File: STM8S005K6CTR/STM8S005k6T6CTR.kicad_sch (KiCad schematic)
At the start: 13 parts, among them IC1 STM8S005K6T6CTR, IC2 L6981C50DR, J1 282837-2

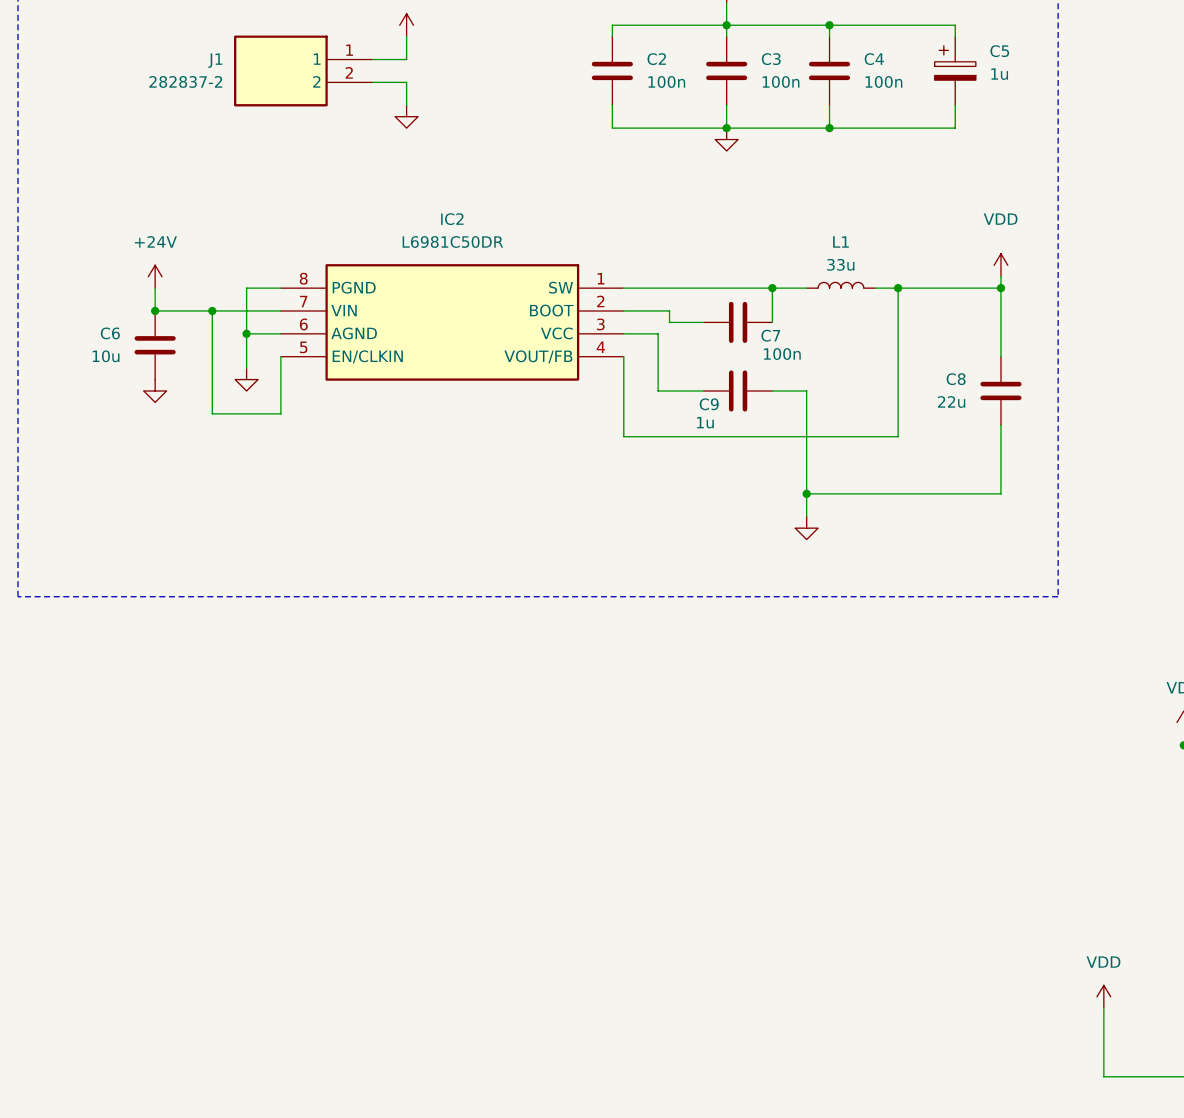
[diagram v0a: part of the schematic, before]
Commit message: [STM8S005K6T6CTR] Calculations: calculated values of components for switching voltage regulator - TI LM2671. Board scheme: Added switching voltage regulator with additional components. Assigned footprints to components.
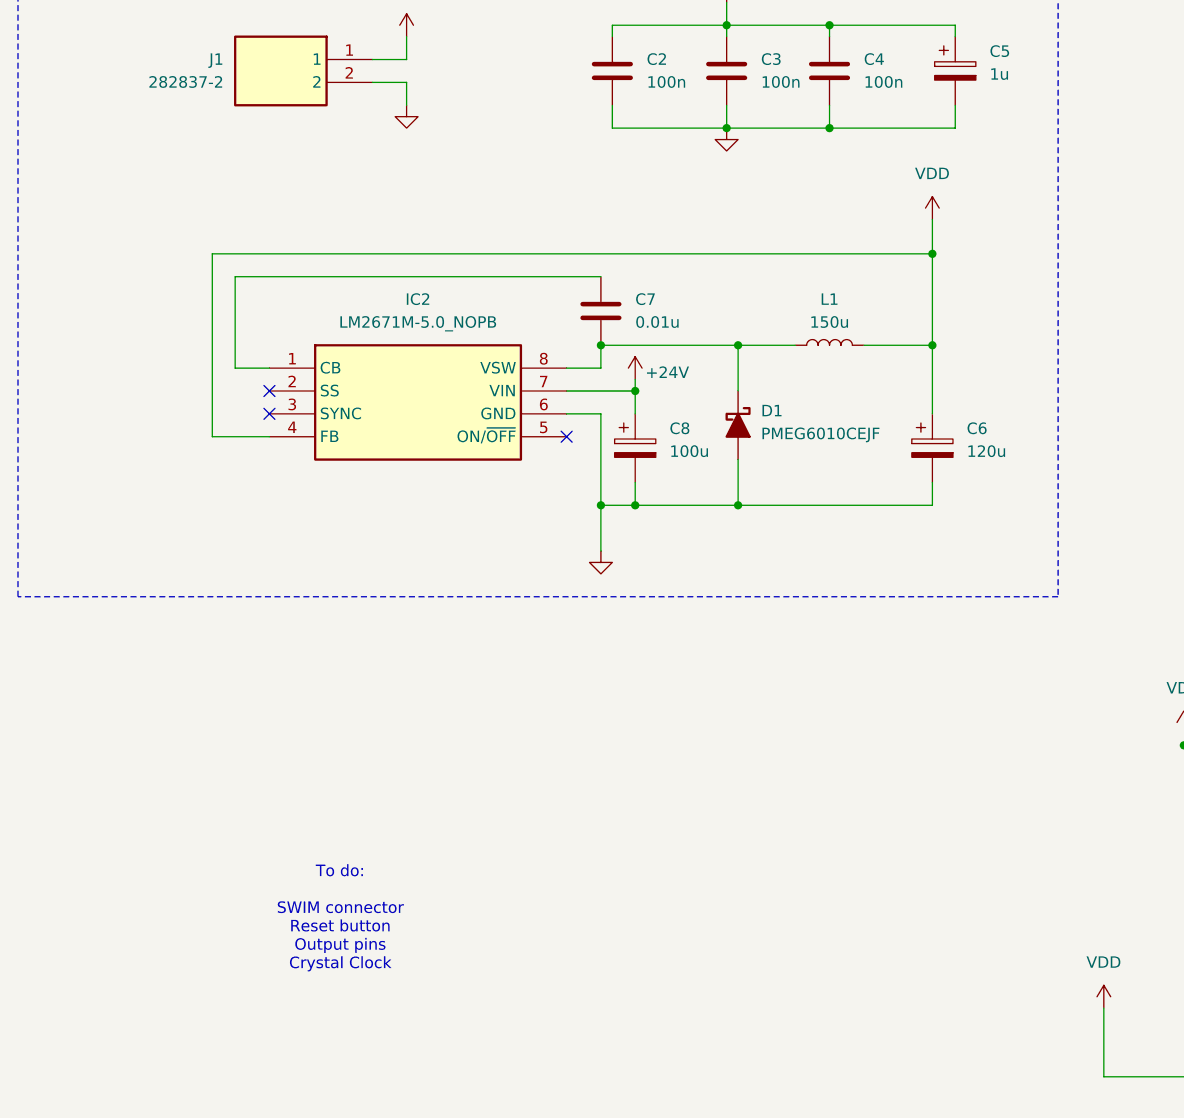
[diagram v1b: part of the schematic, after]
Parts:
- removed C6: 10u, symbol Device:C
- removed C8: 22u, symbol Device:C
- removed C9: 1u, symbol Device:C
- removed IC2: L6981C50DR, SOIC127P600X175-8N, symbol L6981C50DR:L6981C50DR
- added C6: 120u, Capacitor_THT:CP_Radial_D10.0mm_P5.00mm, symbol Device:C_Polarized
- added C8: 100u, Capacitor_THT:CP_Radial_D10.0mm_P5.00mm, symbol Device:C_Polarized
- added D1: PMEG6010CEJF, Diode_SMD:D_SOD-323F, symbol Device:D_Schottky_Filled
- added IC2: LM2671M-5.0_NOPB, SOIC127P600X175-8N, symbol LM2671M-5_0_NOPB:LM2671M-5.0_NOPB
- C7: value 100n -> 0.01u; footprint (none) -> Capacitor_SMD:C_0603_1608Metric
- L1: value 33u -> 150u; footprint (none) -> Wurth_744065151:WE-TPC_1028_103892
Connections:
- net +24V: now also C8.1, IC2.7 (VIN)
- net GND: now also C6.1, C6.2, C8.2, D1.2 (A), IC2.4 (FB), IC2.6 (GND)
- net at C7.2: now also IC2.1 (CB); no longer L1.1
- net at C7.1: now also L1.1, D1.1 (K), IC2.8 (VSW)
- no-connect marks 0 -> 3
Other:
- note added: "To do: SWIM connector Reset button Output pins Crystal Clock"

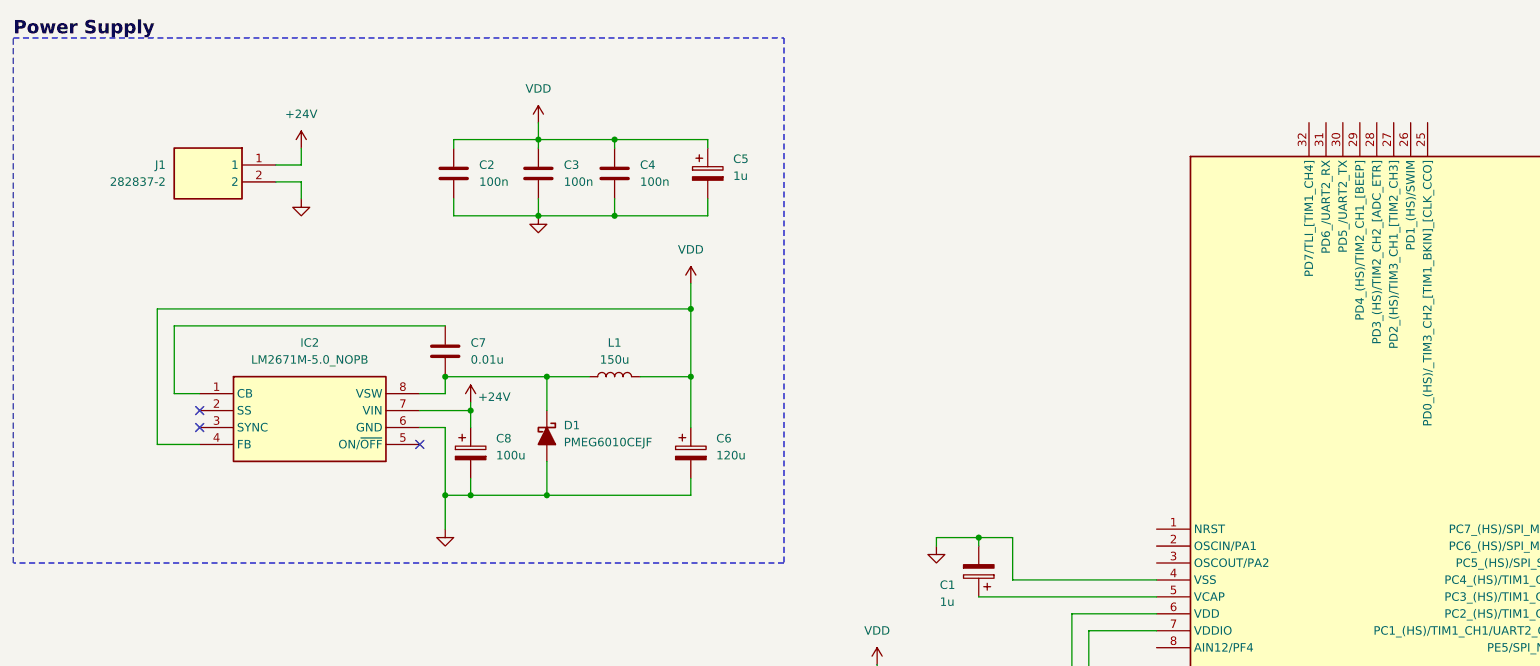
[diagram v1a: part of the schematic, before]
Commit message: [STM8S005K6T6CTR] Board scheme: Added Power Supply Selecection pins. Added SWIM connector.
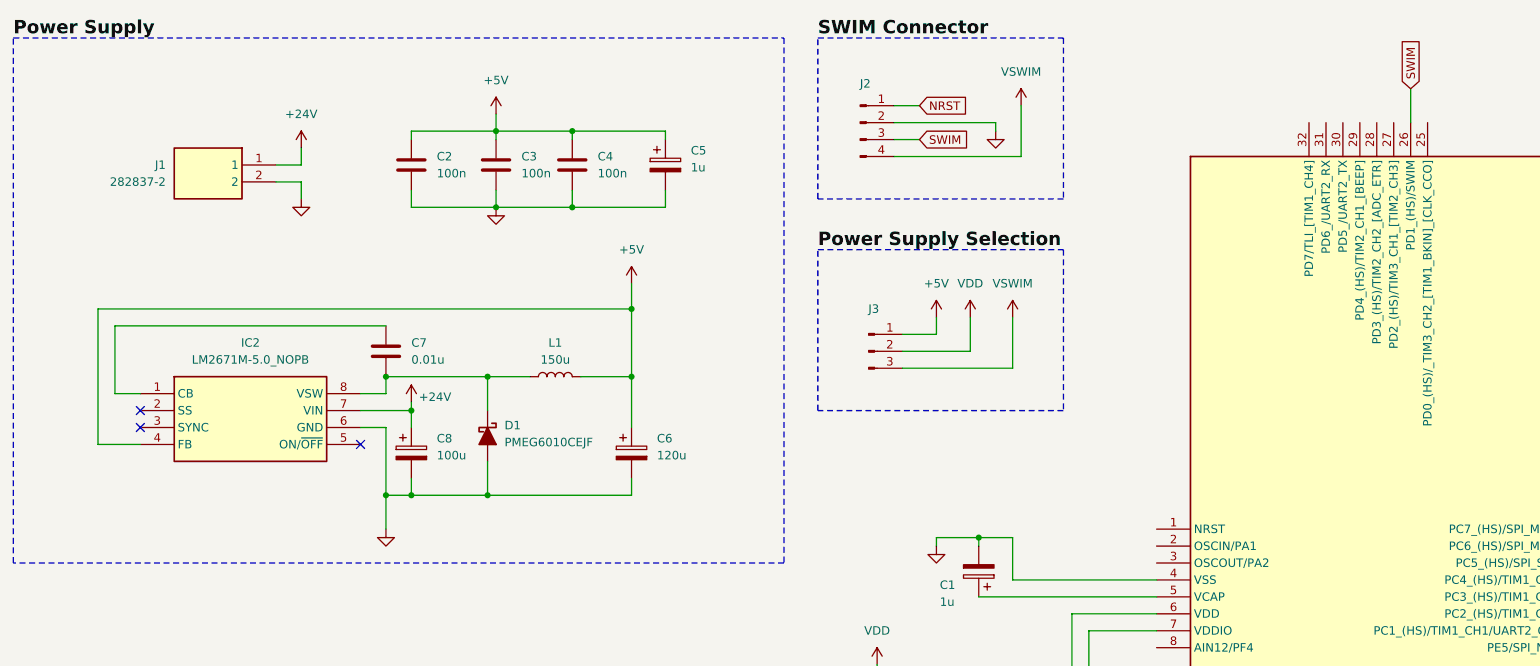
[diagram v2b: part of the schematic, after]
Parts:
- added J2: Conn_01x04_Pin, symbol Connector:Conn_01x04_Pin
- added J3: Conn_01x03_Pin, symbol Connector:Conn_01x03_Pin
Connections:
- net GND: now also J2.2 (Pin_2), J3.2 (Pin_2); no longer C2.1, C3.1, C4.1, C5.1, C6.1, IC2.4 (FB), L1.2
- net SWIM: now reaches IC1.26 (PD1_(HS)/SWIM)
- net SWIM: now also J2.3 (Pin_3)
- new net +5V: C2.1, C3.1, C4.1, C5.1, C6.1, IC2.4 (FB), J3.1 (Pin_1), L1.2
- new net NRST: J2.1 (Pin_1)
- new net VSWIM: J2.4 (Pin_4), J3.3 (Pin_3)
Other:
- moved on the sheet: C2, C3, C4, C5, C6, C7, C8, D1, IC2, L1

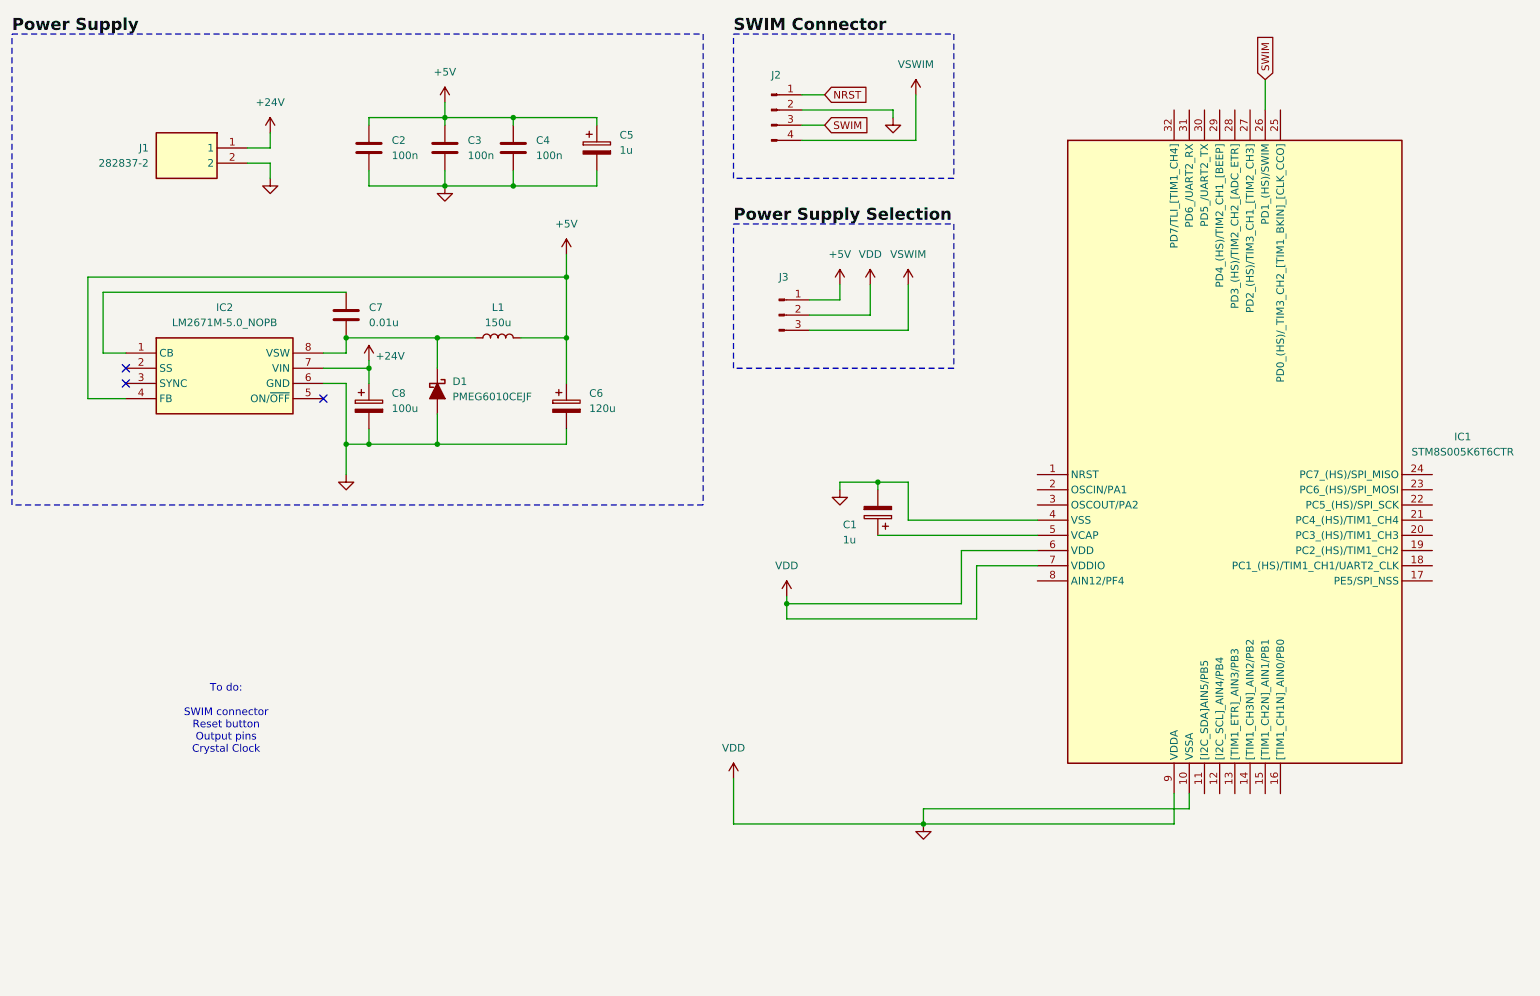
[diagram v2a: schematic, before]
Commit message: [STM8S005K6T6CTR] Calculations: calculated crystal components. Board scheme: Added crystal to scheme (with footprint). Added part of output pins.
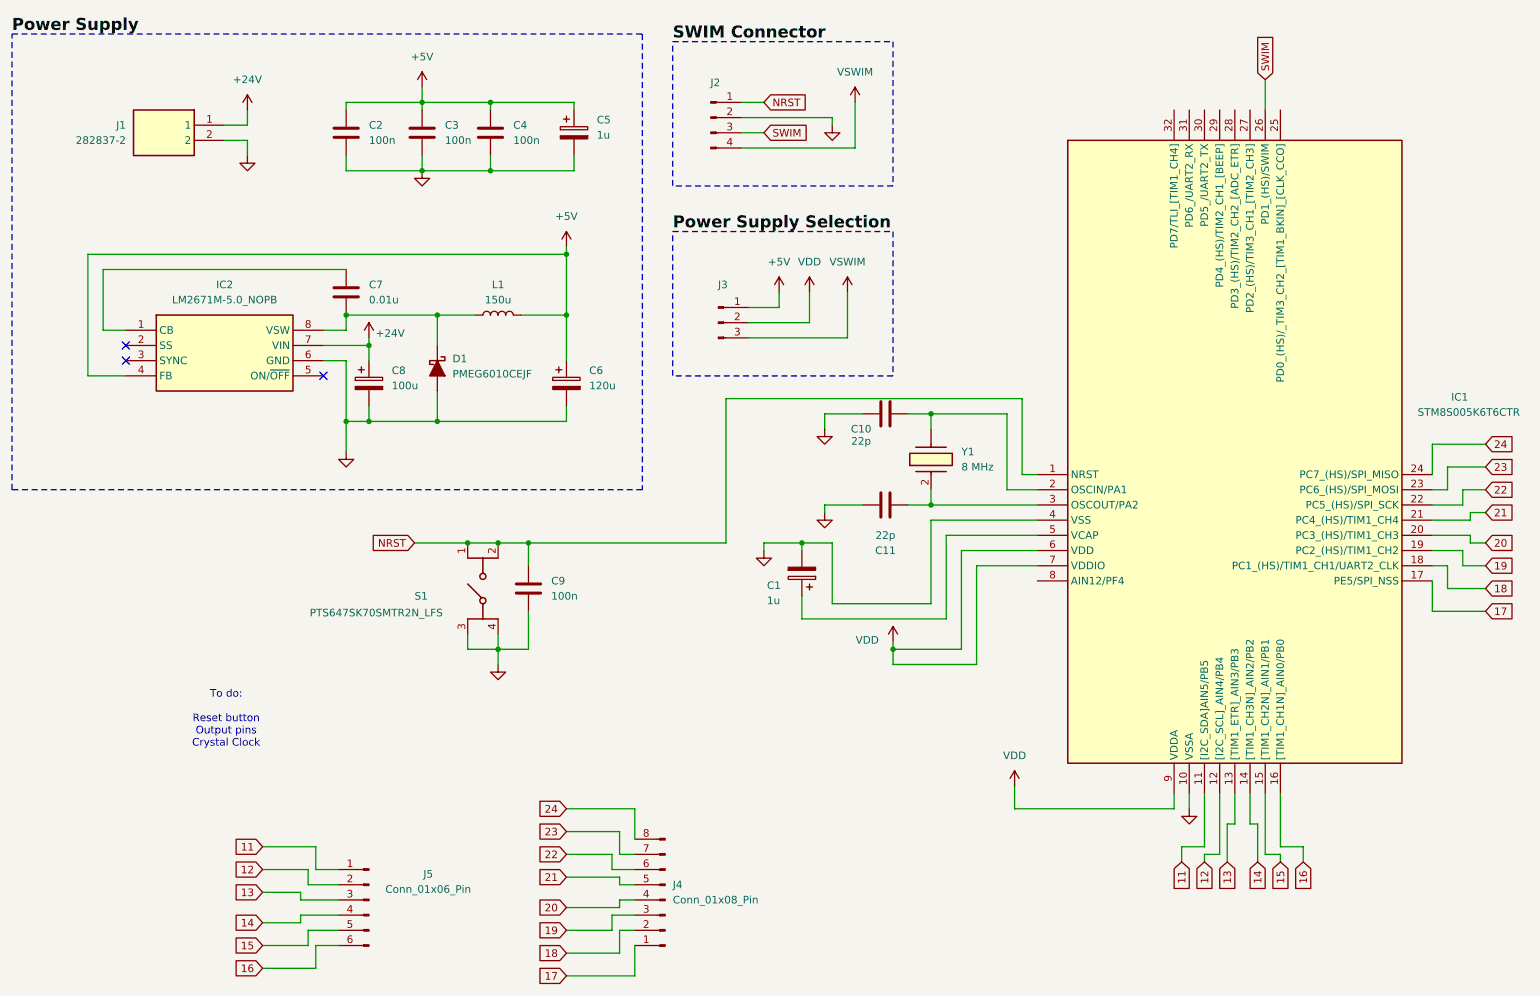
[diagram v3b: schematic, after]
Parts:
- added C10, C11: 22p, symbol Device:C
- added C9: 100n, symbol Device:C
- added J4: Conn_01x08_Pin, symbol Connector:Conn_01x08_Pin
- added J5: Conn_01x06_Pin, symbol Connector:Conn_01x06_Pin
- added S1: PTS647SK70SMTR2N_LFS, PTS647SK70SMTR2N LFS:PTS647SK70SMTR2NLFS, symbol PTS647SK70SMTR2N_LFS:PTS647SK70SMTR2N_LFS
- added Y1: 8 MHz, 830029914_Wurth_8Mhz:830029914, symbol 830029914:830029914
- IC1: footprint QFP80P900X900X160-32N -> STM8S005K6CTR:QFP80P900X900X160-32N
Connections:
- net GND: now also C10.2, C11.2, C9.2, S1.3 (COM_1), S1.4 (COM_2); no longer IC1.6 (VDD), IC1.7 (VDDIO), IC1.9 (VDDA), J3.2 (Pin_2)
- net NRST: now also IC1.1 (NRST), C9.1, S1.1 (NO_1), S1.2 (NO_2)
- net 11: now reaches IC1.11 ([I2C_SDA]AIN5/PB5)
- net 11: now also J5.1 (Pin_1)
- net 12: now reaches IC1.12 ([I2C_SCL]_AIN4/PB4)
- net 12: now also J5.2 (Pin_2)
- net 13: now reaches IC1.13 ([TIM1_ETR]_AIN3/PB3)
- net 13: now also J5.3 (Pin_3)
- net 14: now reaches IC1.14 ([TIM1_CH3N]_AIN2/PB2)
- net 14: now also J5.4 (Pin_4)
- net 15: now reaches IC1.15 ([TIM1_CH2N]_AIN1/PB1)
- net 15: now also J5.5 (Pin_5)
- net 16: now reaches IC1.16 ([TIM1_CH1N]_AIN0/PB0)
- net 16: now also J5.6 (Pin_6)
- net 17: now reaches IC1.17 (PE5/SPI_NSS)
- net 17: now also J4.1 (Pin_1)
- net 18: now reaches IC1.18 (PC1_(HS)/TIM1_CH1/UART2_CLK)
- net 18: now also J4.2 (Pin_2)
- net 19: now reaches IC1.19 (PC2_(HS)/TIM1_CH2)
- net 19: now also J4.3 (Pin_3)
- net at IC1.2 (OSCIN/PA1): now also C10.1, Y1.
- net 20: now reaches IC1.20 (PC3_(HS)/TIM1_CH3)
- net 20: now also J4.4 (Pin_4)
- net 21: now reaches IC1.21 (PC4_(HS)/TIM1_CH4)
- net 21: now also J4.5 (Pin_5)
- net 22: now reaches IC1.22 (PC5_(HS)/SPI_SCK)
- net 22: now also J4.6 (Pin_6)
- net 23: now reaches IC1.23 (PC6_(HS)/SPI_MOSI)
- net 23: now also J4.7 (Pin_7)
- net 24: now reaches IC1.24 (PC7_(HS)/SPI_MISO)
- net 24: now also J4.8 (Pin_8)
- net at IC1.3 (OSCOUT/PA2): now also C11.1, Y1.2 (CRYSTAL__2)
- new net VDD: IC1.6 (VDD), IC1.7 (VDDIO), IC1.9 (VDDA), J3.2 (Pin_2)
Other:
- note added: "To do: Reset button Output pins Crystal Clock"
- note removed: "To do: SWIM connector Reset button Output pins Crystal Clock"
- moved on the sheet: C1, C2, C3, C4, C5, C6, C7, C8, D1, IC2, J1, J2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

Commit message: [STM8S005K6T6CTR] Board scheme: assigned footprints to decoupling capacitors and VCAP capacitor.
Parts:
- removed C1: 1u, symbol Device:C_Polarized
- added C1: 1u, Capacitor_SMD:C_0603_1608Metric, symbol Device:C
- C2, C3, C4, C9: footprint (none) -> Capacitor_SMD:C_0805_2012Metric
- C5: footprint (none) -> Capacitor_THT:CP_Radial_D5.0mm_P2.00mm
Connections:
- net GND: now also C1.1
- net at IC1.5 (VCAP): now also C1.2
